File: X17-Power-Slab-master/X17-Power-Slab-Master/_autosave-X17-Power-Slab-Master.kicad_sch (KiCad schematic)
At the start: 18 parts, among them J2 ET60T-D04-3-08-D04-X-R1-S, J3 796636-6, Q2 IRF1018ESTRLPBF, U1 AZ1117IH-3.3TRG1

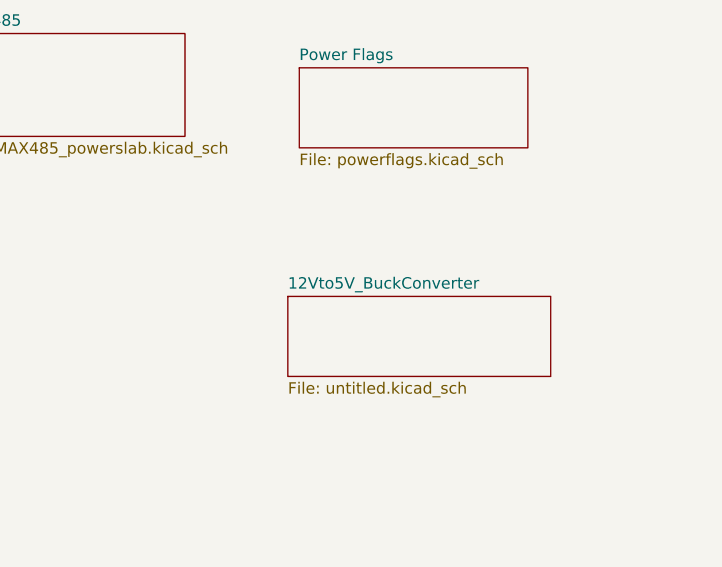
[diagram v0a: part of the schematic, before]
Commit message: Final First(?) Draft
NRST is stuck to general ground for whatever reason.

Test points wont connect for the life of me, will look @ in morning, will have sample plan.

Idea is there, really want to plan it out better 2nd time around. Alumni will give good tips!
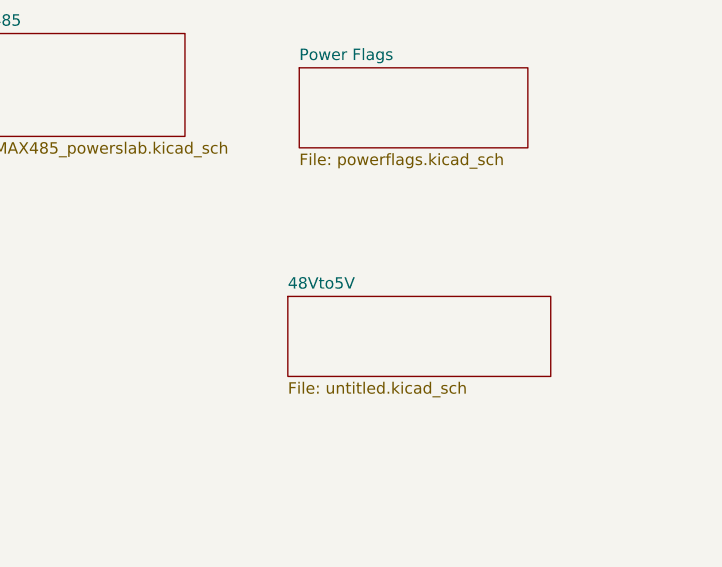
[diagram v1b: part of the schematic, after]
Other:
- sheet 12Vto5V_BuckConverter renamed 48Vto5V
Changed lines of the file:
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@@
 			(color 0 0 0 0.0000)
 		)
-		(property "Sheetname" "12Vto5V_BuckConverter"
+		(property "Sheetname" "48Vto5V"
 			(at 245.11 144.0684 0)
 			(effects
